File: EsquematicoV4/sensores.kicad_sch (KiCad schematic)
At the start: 11 parts, among them U2 MAX98357AETE+

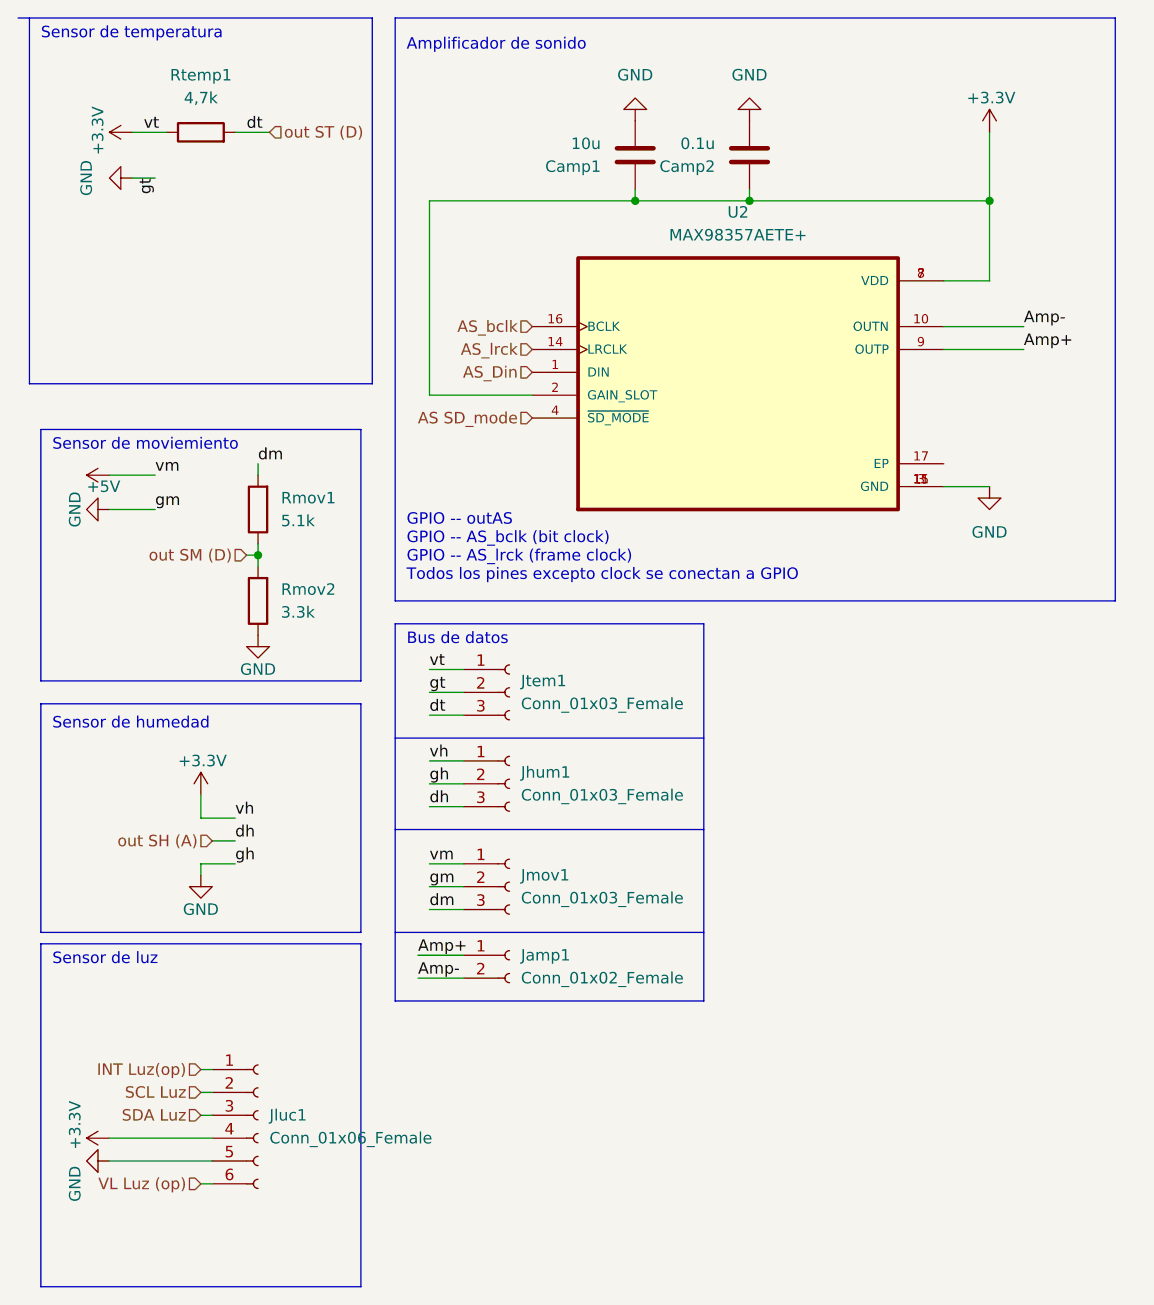
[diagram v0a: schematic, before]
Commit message: Correciones Finales Esquemático - Revisar error con huella del Amplificador de Sonido
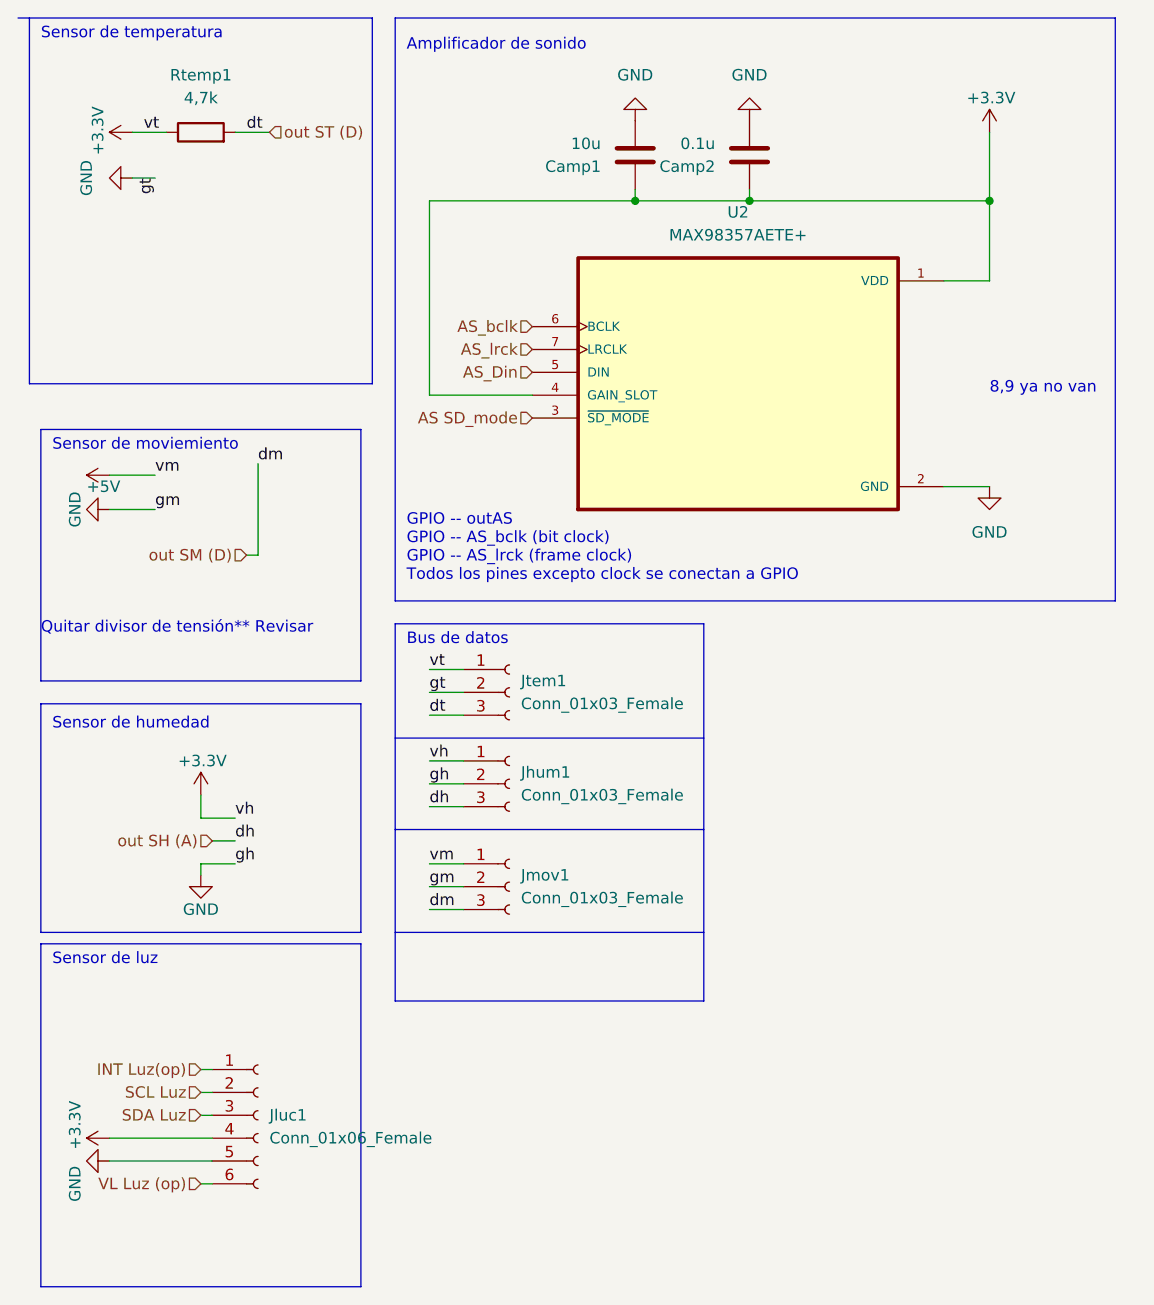
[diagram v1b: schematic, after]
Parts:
- removed Jamp1: Conn_01x02_Female, TerminalBlock_Phoenix:TerminalBlock_Phoenix_MKDS-1,5-2-5.08_1x02_P5.08mm_Horizontal, symbol Connector:Conn_01x02_Female
- removed Rmov1: 5.1k, Resistor_SMD:R_0805_2012Metric_Pad1.20x1.40mm_HandSolder, symbol Device:R
- removed Rmov2: 3.3k, Resistor_SMD:R_0805_2012Metric_Pad1.20x1.40mm_HandSolder, symbol Device:R
- Jluc1: footprint Connector_JST:JST_EH_B6B-EH-A_1x06_P2.50mm_Vertical -> Connector_Molex:Molex_KK-396_A-41791-0006_1x06_P3.96mm_Vertical
- U2: footprint open-automation:MAX98357A -> MAX9835_Editado:MAX98357A_ModuloEditado
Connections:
- net dm is gone; now on net out SM (D): Jmov1.3 (Pin_3)
- net +3V3: now also U2.1 (VDD), U2.4 (GAIN_SLOT); no longer U2.2 (GAIN_SLOT), U2.7 (VDD), U2.8 (VDD)
- net AS SD_mode: now also U2.3 (~{SD_MODE}); no longer U2.4 (~{SD_MODE})
- net AS_Din: now also U2.5 (DIN); no longer U2.1 (DIN)
- net AS_bclk: now also U2.6 (BCLK); no longer U2.16 (BCLK)
- net AS_lrck: now also U2.7 (LRCLK); no longer U2.14 (LRCLK)
- net GND: now also U2.2 (GND); no longer U2.11 (GND), U2.15 (GND), U2.3 (GND)
- removed net Amp+: U2.9 (OUTP)
- removed net Amp-: U2.10 (OUTN)
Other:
- note added: "8,9 ya no van"
- note added: "Quitar divisor de tensión** Revisar"

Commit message: PCB organizada para autoruteo
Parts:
- U2: footprint MAX9835_Editado:MAX98357A_ModuloEditado -> MAX9835_EditadoLib:MAX98357A_ModuloEditado
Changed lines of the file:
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@@
     (property "Reference" "U2" (id 0) (at 99.06 40.64 0))
     (property "Value" "MAX98357AETE+" (id 1) (at 99.06 43.18 0))
-    (property "Footprint" "MAX9835_Editado:MAX98357A_ModuloEditado" (id 2) (at 99.06 58.42 0)
+    (property "Footprint" "MAX9835_EditadoLib:MAX98357A_ModuloEditado" (id 2) (at 99.06 58.42 0)
       (effects (font (size 1.27 1.27)) (justify left bottom) hide)
     )
